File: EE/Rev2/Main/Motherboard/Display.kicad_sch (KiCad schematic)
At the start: 1 part, among them J9 Conn_01x06

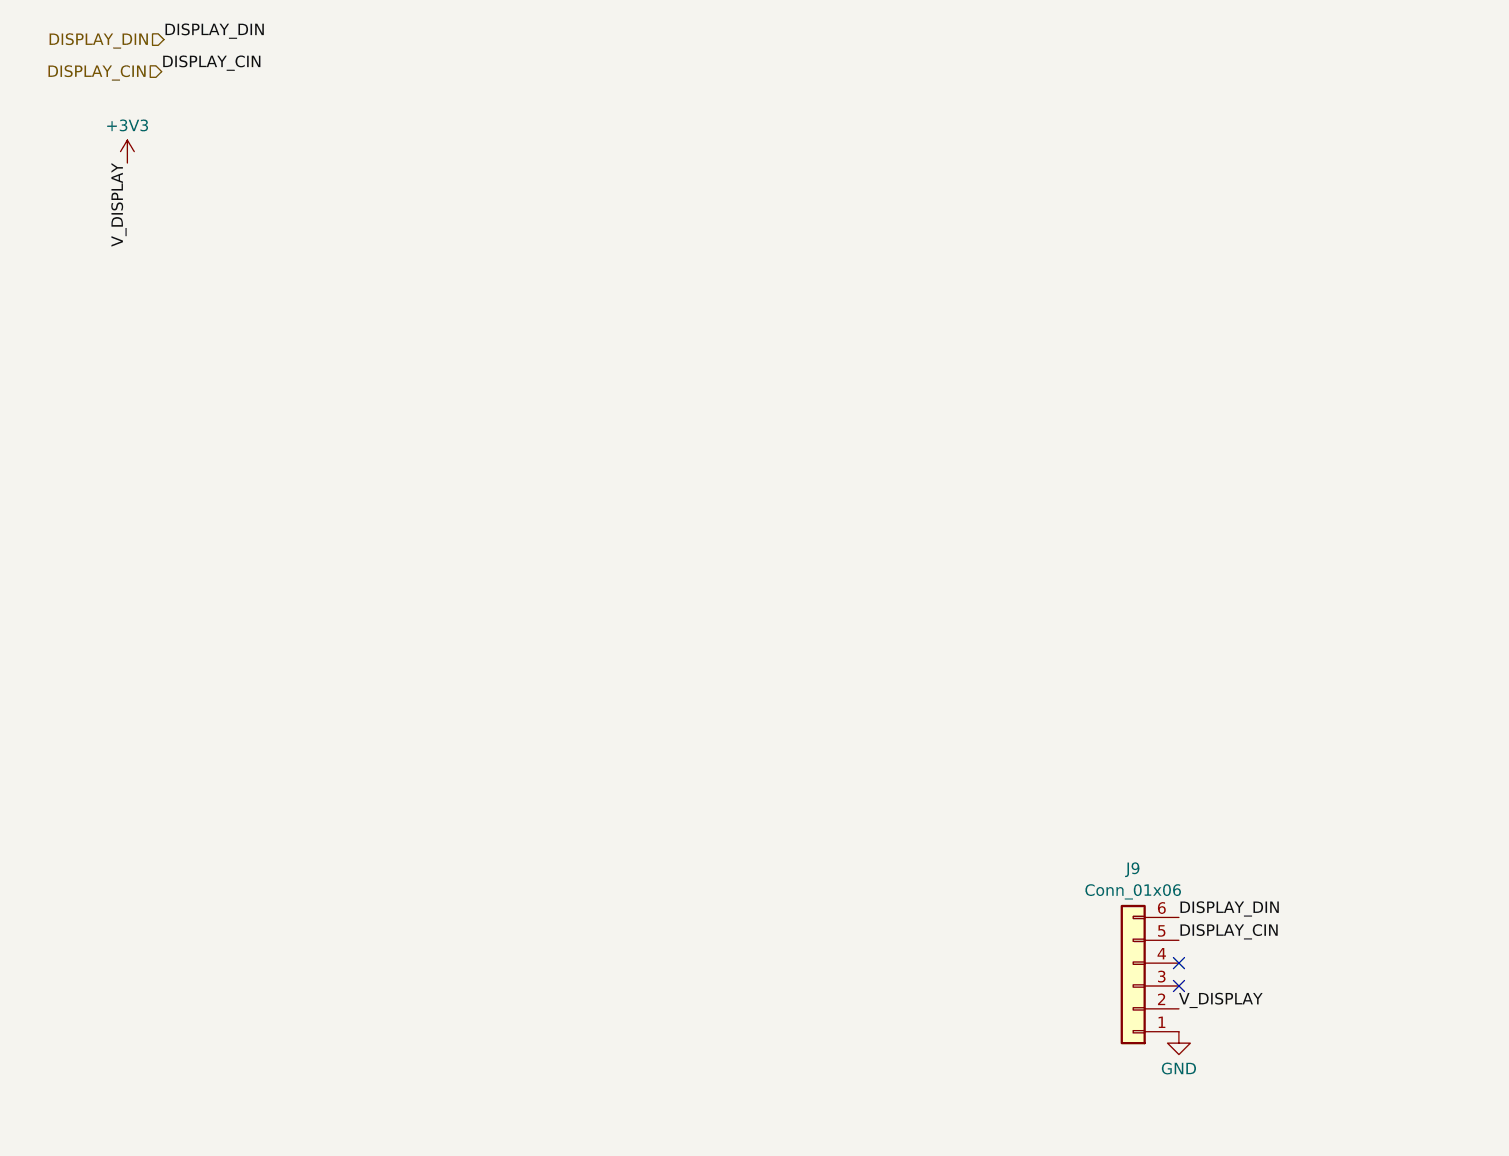
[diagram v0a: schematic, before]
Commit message: Updating Format, Adding Rev2 Start
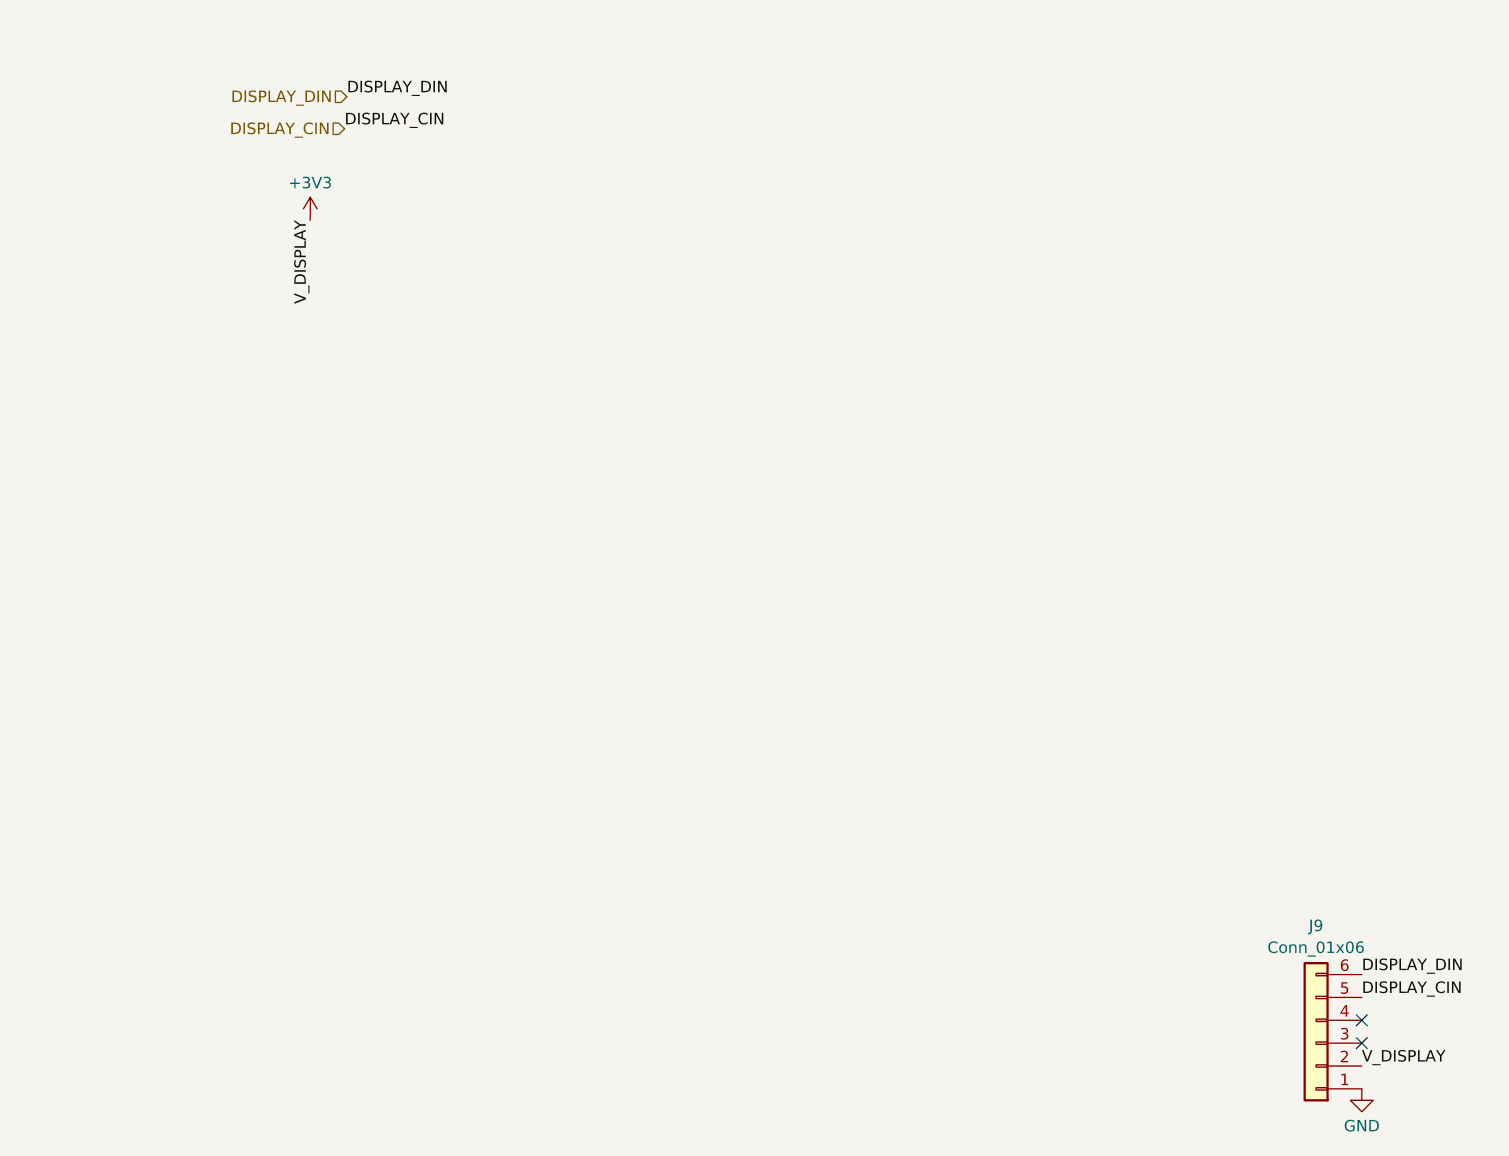
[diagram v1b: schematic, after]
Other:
- moved on the sheet: J9
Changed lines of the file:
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@@
 	(paper "A4")
 	(no_connect
-		(at 138.43 125.73)
+		(at 158.75 132.08)
 	)
 	(no_connect
-		(at 138.43 128.27)
+		(at 158.75 134.62)
+	)
+	(label "V_DISPLAY"
+		(at 41.91 43.18 270)
+		(effects
+			(font
+				(size 1.27 1.27)
+			)
+			(justify right bottom)
+		)
+	)
+	(label "DISPLAY_CIN"
+		(at 158.75 129.54 0)
+		(effects
+			(font
+				(size 1.27 1.27)
+			)
+			(justify left bottom)
+		)
+	)
+	(label "DISPLAY_CIN"
+		(at 45.72 33.02 0)
+		(effects
+			(font
+				(size 1.27 1.27)
+			)
+			(justify left bottom)
+		)
 	)
 	(label "DISPLAY_DIN"
-		(at 25.654 23.114 0)
-		(effects
-			(font
-				(size 1.27 1.27)
-			)
-			(justify left bottom)
-		)
-	)
-	(label "DISPLAY_CIN"
-		(at 138.43 123.19 0)
+		(at 45.974 29.464 0)
 		(effects
 			(font
@@
 	)
 	(label "DISPLAY_DIN"
-		(at 138.43 120.65 0)
-		(effects
-			(font
-				(size 1.27 1.27)
-			)
-			(justify left bottom)
-		)
-	)
-	(label "DISPLAY_CIN"
-		(at 25.4 26.67 0)
+		(at 158.75 127 0)
 		(effects
 			(font
@@
 	)
 	(label "V_DISPLAY"
-		(at 138.43 130.81 0)
-		(effects
-			(font
-				(size 1.27 1.27)
-			)
-			(justify left bottom)
-		)
-	)
-	(label "V_DISPLAY"
-		(at 21.59 36.83 270)
-		(effects
-			(font
-				(size 1.27 1.27)
-			)
-			(justify right bottom)
+		(at 158.75 137.16 0)
+		(effects
+			(font
+				(size 1.27 1.27)
+			)
+			(justify left bottom)
+		)
+	)
+	(hierarchical_label "DISPLAY_CIN"
+		(shape input)
+		(at 45.72 33.02 180)
+		(effects
+			(font
+				(size 1.27 1.27)
+			)
+			(justify right)
 		)
 	)
 	(hierarchical_label "DISPLAY_DIN"
 		(shape input)
-		(at 25.654 23.114 180)
-		(effects
-			(font
-				(size 1.27 1.27)
-			)
-			(justify right)
-		)
-	)
-	(hierarchical_label "DISPLAY_CIN"
-		(shape input)
-		(at 25.4 26.67 180)
+		(at 45.974 29.464 180)
 		(effects
 			(font
@@
 	(symbol
 		(lib_id "Connector_Generic:Conn_01x06")
-		(at 133.35 128.27 180)
+		(at 153.67 134.62 180)
 		(unit 1)
 		(exclude_from_sim no)
@@
 		(fields_autoplaced yes)
 		(property "Reference" "J9"
-			(at 133.35 115.2355 0)
+			(at 153.67 121.5855 0)
 			(effects
 				(font
@@
 		)
 		(property "Value" "Conn_01x06"
-			(at 133.35 117.6598 0)
+			(at 153.67 124.0098 0)
 			(effects
 				(font
@@
 		)
 		(property "Footprint" "Library:RGB_7Segment"
-			(at 133.35 128.27 0)
+			(at 153.67 134.62 0)
 			(effects
 				(font
@@
 		)
 		(property "Datasheet" "~"
-			(at 133.35 128.27 0)
+			(at 153.67 134.62 0)
 			(effects
 				(font
@@
 		)
 		(property "Description" "Generic connector, single row, 01x06, script generated (kicad-library-utils/schlib/autogen/connector/)"
-			(at 133.35 128.27 0)
+			(at 153.67 134.62 0)
 			(effects
 				(font
@@
 		)
 		(instances
-			(project ""
-				(path "/dfe0084c-a900-4f47-8966-915ebf3a8e75/8b04ffa1-873f-4cda-b1fe-4981fdbc7b42"
+			(project "Motherboard"
+				(path "/86871609-316a-48ec-ba57-1907879b4887/bdf23807-ee07-4758-a3ed-c502a290e5f4"
 					(reference "J9")
 					(unit 1)
@@
 	(symbol
 		(lib_id "power:+3V3")
-		(at 21.59 36.83 0)
+		(at 41.91 43.18 0)
 		(unit 1)
 		(exclude_from_sim no)
@@
 		(fields_autoplaced yes)
 		(property "Reference" "#PWR02"
-			(at 21.59 40.64 0)
+			(at 41.91 46.99 0)
 			(effects
 				(font
@@
 		)
 		(property "Value" "+3V3"
-			(at 21.59 32.6969 0)
+			(at 41.91 39.0469 0)
 			(effects
 				(font
@@
 		)
 		(property "Footprint" ""
-			(at 21.59 36.83 0)
+			(at 41.91 43.18 0)
 			(effects
 				(font
@@
 		)
 		(property "Datasheet" ""
-			(at 21.59 36.83 0)
+			(at 41.91 43.18 0)
 			(effects
 				(font
@@
 		)
 		(property "Description" "Power symbol creates a global label with name \"+3V3\""
-			(at 21.59 36.83 0)
+			(at 41.91 43.18 0)
 			(effects
 				(font
@@
 		)
 		(instances
-			(project ""
-				(path "/dfe0084c-a900-4f47-8966-915ebf3a8e75/8b04ffa1-873f-4cda-b1fe-4981fdbc7b42"
+			(project "Motherboard"
+				(path "/86871609-316a-48ec-ba57-1907879b4887/bdf23807-ee07-4758-a3ed-c502a290e5f4"
 					(reference "#PWR02")
 					(unit 1)
@@
 	(symbol
 		(lib_id "power:GND")
-		(at 138.43 133.35 0)
+		(at 158.75 139.7 0)
 		(unit 1)
 		(exclude_from_sim no)
@@
 		(fields_autoplaced yes)
 		(property "Reference" "#PWR028"
-			(at 138.43 139.7 0)
+			(at 158.75 146.05 0)
 			(effects
 				(font
@@
 		)
 		(property "Value" "GND"
-			(at 138.43 137.4831 0)
+			(at 158.75 143.8331 0)
 			(effects
 				(font
@@
 		)
 		(property "Footprint" ""
-			(at 138.43 133.35 0)
+			(at 158.75 139.7 0)
 			(effects
 				(font
@@
 		)
 		(property "Datasheet" ""
-			(at 138.43 133.35 0)
+			(at 158.75 139.7 0)
 			(effects
 				(font
@@
 		)
 		(property "Description" ""
-			(at 138.43 133.35 0)
+			(at 158.75 139.7 0)
 			(effects
 				(font
@@
 		)
 		(instances
-			(project "MainBoard"
-				(path "/dfe0084c-a900-4f47-8966-915ebf3a8e75/8b04ffa1-873f-4cda-b1fe-4981fdbc7b42"
+			(project "Motherboard"
+				(path "/86871609-316a-48ec-ba57-1907879b4887/bdf23807-ee07-4758-a3ed-c502a290e5f4"
 					(reference "#PWR028")
 					(unit 1)
